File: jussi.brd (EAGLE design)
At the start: 88.9 x 50.8 mm, 3 parts

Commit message: "Done"
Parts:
- added D1, D10, D11, D12, D13, D14, D15, D16, D2, D3, D4, D5, D6, D7, D8, D9: P47FV2BB-24-1, pcb-card:P47F
- added MISO, MOSI, RESET, SCK: TPTP08R, testpad:TP08R
- added R1, R2, R3, R4, R5, R6, R7, R8: RES14_16, dubec:0402
- added U$1: ATTINY2/4/84AMU, pcb-card:20-WFQFN
- added U$2: (no value), dubec:0805
- D+, D-: value TPTP06R -> TPTP08R; device testpad:TP06R -> testpad:TP08R
- flipped D+ to the bottom
- flipped D- to the bottom
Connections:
- new net DN1: R1.2, U$1.3
- new net DN2: R2.2, U$1.4
- new net DN3: R3.2, U$1.5
- new net DN4: R4.2, U$1.11
- new net DN5: R5.2, U$1.12
- new net DN6: R6.2, U$1.14
- new net DN7: R7.2, U$1.15
- new net DN8: R8.2, U$1.2
- new net MISO: MISO.TP, U$1.20
- new net MOSI: MOSI.TP, U$1.16
- new net N$1: D1.C, D2.A
- new net N$10: D3.A, R2.1
- new net N$11: D5.A, R3.1
- new net N$12: D7.A, R4.1
- new net N$13: D9.A, R5.1
- new net N$14: D11.A, R6.1
- new net N$15: D13.A, R7.1
- new net N$16: D15.A, R8.1
- new net N$2: D3.C, D4.A
- new net N$3: D5.C, D6.A
- new net N$4: D7.C, D8.A
- new net N$5: D10.A, D9.C
- new net N$6: D11.C, D12.A
- new net N$7: D13.C, D14.A
- new net N$8: D15.C, D16.A
- new net N$9: D1.A, R1.1
- new net RESET: RESET.TP, U$1.13
- new net SCK: SCK.TP, U$1.1
- new net USB_GND: JP1.GND
- net GND: now also D10.C, D12.C, D14.C, D16.C, D2.C, D4.C, D6.C, D8.C, U$1.8, U$1.PAD, U$2.2; no longer JP1.GND
- net VIN: now also U$1.9, U$2.1
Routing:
- net N$16: track 0.00 -> 70.3 mm
- net VIN: track 0.00 -> 46.9 mm, vias 0 -> 3
- net N$15: track 0.00 -> 46.2 mm
- net N$14: track 0.00 -> 32.9 mm
- net N$9: track 0.00 -> 21.4 mm
- net N$7: track 0.00 -> 20.6 mm
- net N$13: track 0.00 -> 19.9 mm
- net N$10: track 0.00 -> 13.9 mm
- net N$2: track 0.00 -> 13.8 mm
- net N$4: track 0.00 -> 13.0 mm
- net N$8: track 0.00 -> 12.1 mm
- net N$6: track 0.00 -> 11.9 mm
- net N$5: track 0.00 -> 11.1 mm
- net N$3: track 0.00 -> 9.18 mm
- net GND: track 0.00 -> 8.12 mm, vias 0 -> 7
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- added copper zone on layer 1, net GND
- added copper zone on layer 16, net GND
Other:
- outline, holes or cut-outs redrawn

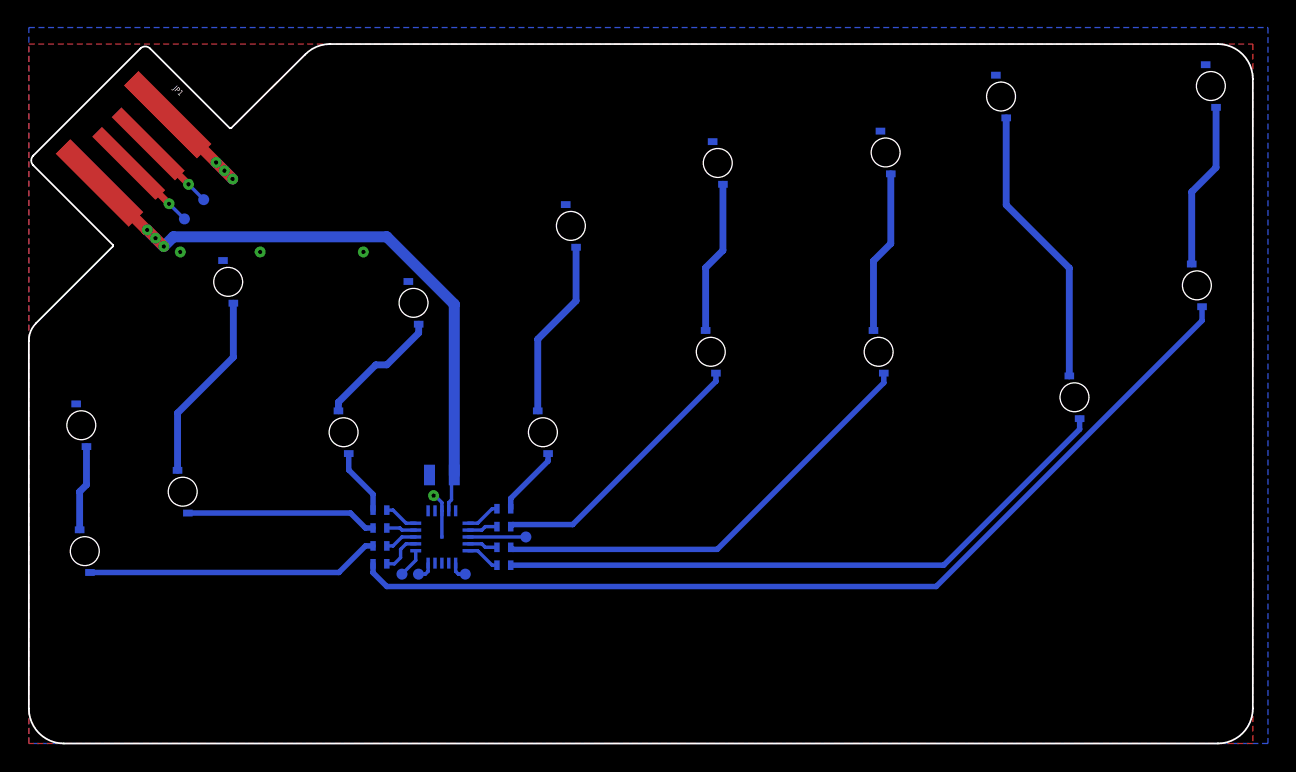
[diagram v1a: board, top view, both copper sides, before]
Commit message: Copper closer to holes
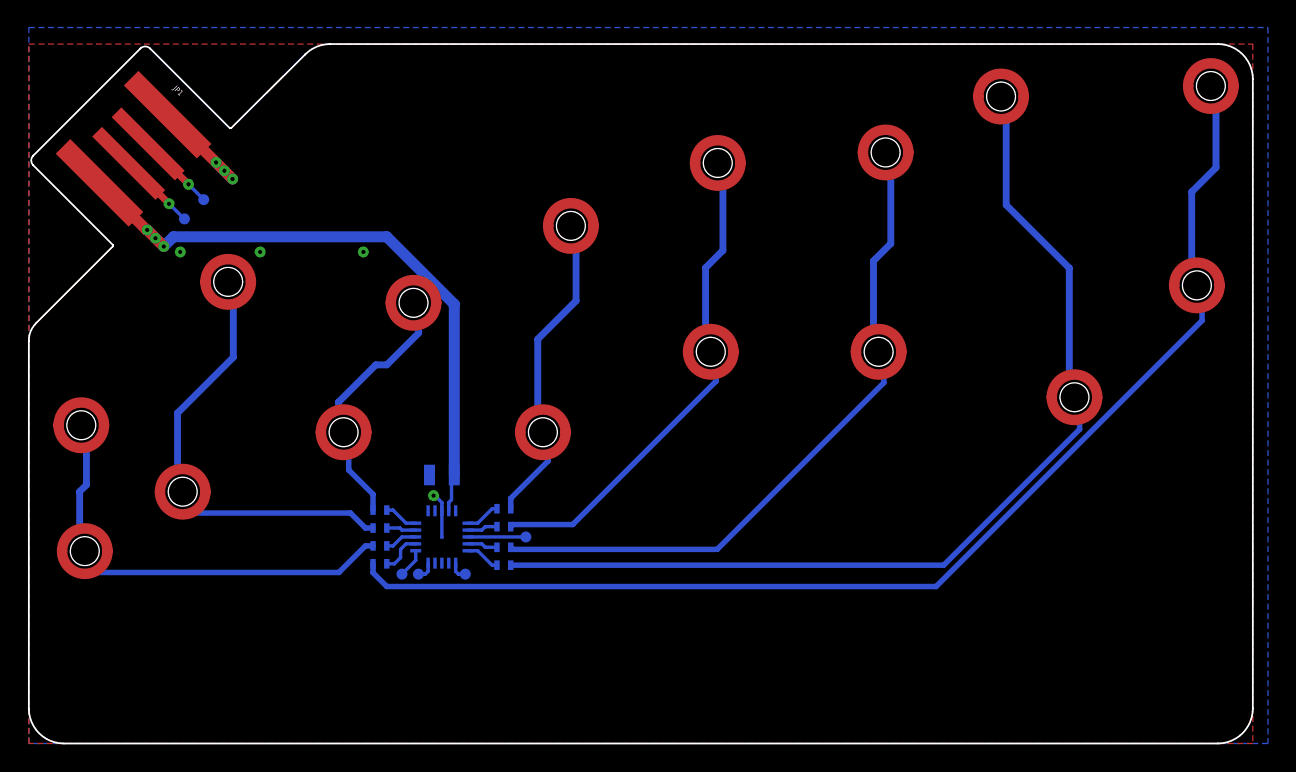
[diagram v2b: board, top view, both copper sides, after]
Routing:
- net GND: track 8.12 -> 113.8 mm

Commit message: Zip generated
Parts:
- added GND, VCC: TPTP08R, testpad:TP08R
- moved D- 1.27 mm to (12.2, 37.2)
- moved D+ 1.26 mm to (13.6, 38.6)
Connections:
- net GND: now also GND.TP
- net VIN: now also VCC.TP
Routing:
- net VIN: track 46.9 -> 49.3 mm
- net D-: track 5.71 -> 6.99 mm
- net D+: track 5.71 -> 6.97 mm
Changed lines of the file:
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@@
 <wire x1="49.9" y1="26.3" x2="39.5" y2="15.9" width="0.3" layer="30"/>
 <wire x1="39.5" y1="15.9" x2="35.75" y2="15.9" width="0.3" layer="30"/>
-<wire x1="8.6" y1="37.3" x2="9.8" y2="36.1" width="0.6" layer="30"/>
 <wire x1="3.7" y1="15.775" x2="3.7" y2="18.325" width="0.4" layer="30"/>
 <wire x1="3.7" y1="18.325" x2="4.175" y2="18.8" width="0.4" layer="30"/>
@@
 <elements>
 <element name="JP1" library="SparkFun-Connectors" package="USB-A-PCB" value="USBPCB" x="7.747" y="43.053" rot="R315"/>
-<element name="D+" library="testpad" package="TP08R" value="TPTP08R" x="12.7" y="39.5" rot="MR0">
-<attribute name="TP_SIGNAL_NAME" value="" x="12.7" y="39.5" size="1.778" layer="28" rot="MR0" display="off"/>
-</element>
-<element name="D-" library="testpad" package="TP08R" value="TPTP08R" x="11.3" y="38.1" rot="MR0">
-<attribute name="TP_SIGNAL_NAME" value="" x="11.3" y="38.1" size="1.778" layer="28" rot="MR0" display="off"/>
+<element name="D+" library="testpad" package="TP08R" value="TPTP08R" x="13.625" y="38.65" rot="MR0">
+<attribute name="TP_SIGNAL_NAME" value="" x="13.625" y="38.65" size="1.778" layer="28" rot="MR0" display="off"/>
+</element>
+<element name="D-" library="testpad" package="TP08R" value="TPTP08R" x="12.2" y="37.2" rot="MR0">
+<attribute name="TP_SIGNAL_NAME" value="" x="12.2" y="37.2" size="1.778" layer="28" rot="MR0" display="off"/>
 </element>
 <element name="D1" library="pcb-card" package="P47F" value="P47FV2BB-24-1" x="4.064" y="13.97" rot="R270">
@@
 <element name="RESET" library="testpad" package="TP08R" value="TPTP08R" x="36.1" y="15" rot="MR0">
 <attribute name="TP_SIGNAL_NAME" value="" x="36.1" y="15" size="1.778" layer="28" rot="MR0" display="off"/>
+</element>
+<element name="VCC" library="testpad" package="TP08R" value="TPTP08R" x="33" y="19" rot="MR0">
+<attribute name="TP_SIGNAL_NAME" value="" x="33" y="19" size="1.778" layer="28" rot="MR0" display="off"/>
+</element>
+<element name="GND" library="testpad" package="TP08R" value="TPTP08R" x="27" y="19" rot="MR0">
+<attribute name="TP_SIGNAL_NAME" value="" x="27" y="19" size="1.778" layer="28" rot="MR0" display="off"/>
 </element>
 </elements>
@@
 <wire x1="30" y1="15" x2="30" y2="16.9" width="0.25" layer="16"/>
 <via x="29.4" y="18" extent="1-16" drill="0.3"/>
-<via x="16.8" y="35.7" extent="1-16" drill="0.3"/>
-<via x="24.3" y="35.7" extent="1-16" drill="0.3"/>
-<via x="11" y="35.7" extent="1-16" drill="0.3"/>
+<via x="17.3" y="35" extent="1-16" drill="0.3"/>
+<via x="24.3" y="35" extent="1-16" drill="0.3"/>
 <contactref element="U$2" pad="2"/>
 <wire x1="30" y1="16.9" x2="30" y2="17.5" width="0.25" layer="16"/>
@@
 <wire x1="84.201" y1="47.752" x2="87.503" y2="47.752" width="0.762" layer="1" curve="-180"/>
 <wire x1="87.503" y1="47.752" x2="84.201" y2="47.752" width="0.762" layer="1" curve="-180"/>
+<via x="29.8" y="20.9" extent="1-16" drill="0.3"/>
+<contactref element="GND" pad="TP"/>
 <wire x1="85.477" y1="49.302" x2="84.201" y2="47.752" width="0" layer="19" extent="1-16"/>
+<wire x1="16.129" y1="33.528" x2="17.3" y2="35" width="0" layer="19" extent="1-1"/>
 <wire x1="68.961" y1="46.99" x2="70.237" y2="48.54" width="0" layer="19" extent="1-16"/>
 <wire x1="60.579" y1="42.926" x2="61.855" y2="44.476" width="0" layer="19" extent="1-16"/>
@@
 <wire x1="37.719" y1="37.592" x2="38.995" y2="39.142" width="0" layer="19" extent="1-16"/>
 <wire x1="26.289" y1="32.004" x2="27.565" y2="33.554" width="0" layer="19" extent="1-16"/>
-<wire x1="12.827" y1="33.528" x2="14.103" y2="35.078" width="0" layer="19" extent="1-16"/>
 <wire x1="2.159" y1="23.114" x2="3.435" y2="24.664" width="0" layer="19" extent="1-16"/>
-<wire x1="24.511" y1="22.606" x2="29.1" y2="19.5" width="0" layer="19" extent="1-16"/>
+<wire x1="24.511" y1="22.606" x2="27" y2="19" width="0" layer="19" extent="1-16"/>
+<wire x1="35.687" y1="22.606" x2="29.8" y2="20.9" width="0" layer="19" extent="1-1"/>
 <wire x1="9.525" y1="18.288" x2="5.461" y2="23.114" width="0" layer="19" extent="1-1"/>
 <wire x1="5.715" y1="13.97" x2="9.525" y2="18.288" width="0" layer="19" extent="1-1"/>
-<wire x1="35.687" y1="22.606" x2="29.1" y2="19.5" width="0" layer="19" extent="1-16"/>
 <wire x1="47.879" y1="28.448" x2="38.989" y2="22.606" width="0" layer="19" extent="1-1"/>
 <wire x1="60.071" y1="28.448" x2="51.181" y2="28.448" width="0" layer="19" extent="1-1"/>
@@
 <wire x1="9.2" y1="36.7" x2="9.8" y2="36.1" width="0.8" layer="16"/>
 <contactref element="U$1" pad="9"/>
-<wire x1="9.8" y1="36.1" x2="10.5" y2="36.8" width="0.8" layer="16"/>
-<wire x1="10.5" y1="36.8" x2="26" y2="36.8" width="0.8" layer="16"/>
-<wire x1="26" y1="36.8" x2="30.9" y2="31.9" width="0.8" layer="16"/>
+<wire x1="26.7" y1="36.1" x2="30.9" y2="31.9" width="0.8" layer="16"/>
 <wire x1="30.9" y1="31.9" x2="30.9" y2="19.5" width="0.8" layer="16"/>
 <wire x1="30.5" y1="16.9" x2="30.5" y2="17.5" width="0.25" layer="16"/>
@@
 <wire x1="30.7" y1="17.7" x2="30.7" y2="19.3" width="0.25" layer="16"/>
 <wire x1="30.7" y1="19.3" x2="30.9" y2="19.5" width="0.25" layer="16"/>
+<wire x1="9.8" y1="36.1" x2="12.9" y2="36.1" width="0.8" layer="16"/>
+<wire x1="12.9" y1="36.1" x2="13.4" y2="36.6" width="0.8" layer="16"/>
+<wire x1="13.4" y1="36.6" x2="14.8" y2="36.6" width="0.8" layer="16"/>
+<wire x1="14.8" y1="36.6" x2="15.3" y2="36.1" width="0.8" layer="16"/>
+<wire x1="15.3" y1="36.1" x2="26.7" y2="36.1" width="0.8" layer="16"/>
+<contactref element="VCC" pad="TP"/>
+<wire x1="33" y1="19" x2="30.9" y2="19" width="0.25" layer="16"/>
+<wire x1="30.9" y1="19" x2="30.9" y2="19.5" width="0.25" layer="16"/>
 </signal>
 <signal name="D+">
@@
 <contactref element="D+" pad="TP"/>
 <wire x1="8.6662375" y1="43.547971875" x2="11.6" y2="40.614209375" width="0.5" layer="1"/>
-<wire x1="11.6" y1="40.614209375" x2="12.7" y2="39.5" width="0.25" layer="16"/>
+<wire x1="11.6" y1="40.614209375" x2="13.625" y2="38.65" width="0.25" layer="16"/>
 <via x="11.6" y="40.614209375" extent="1-16" drill="0.3"/>
 </signal>
@@
 <contactref element="D-" pad="TP"/>
 <wire x1="7.252025" y1="42.133759375" x2="10.185784375" y2="39.2" width="0.5" layer="1"/>
-<wire x1="10.185784375" y1="39.2" x2="11.3" y2="38.1" width="0.25" layer="16"/>
+<wire x1="10.185784375" y1="39.2" x2="12.2" y2="37.2" width="0.25" layer="16"/>
 <via x="10.185784375" y="39.2" extent="1-16" drill="0.3"/>
 </signal>
